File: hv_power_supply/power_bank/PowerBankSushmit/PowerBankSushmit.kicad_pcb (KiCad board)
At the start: 2 copper layers, 43 parts, among them J1 NanoFit_RA_TH_02, J2 NanoFit_RA_TH_02, J3 USB-A-S-X-X-SM2, Q1 SSM3K333R, U1 USB_MicroB, U2 MCP73871T-2CCI_ML, U3 - Boost Converter TPS61090RSAR

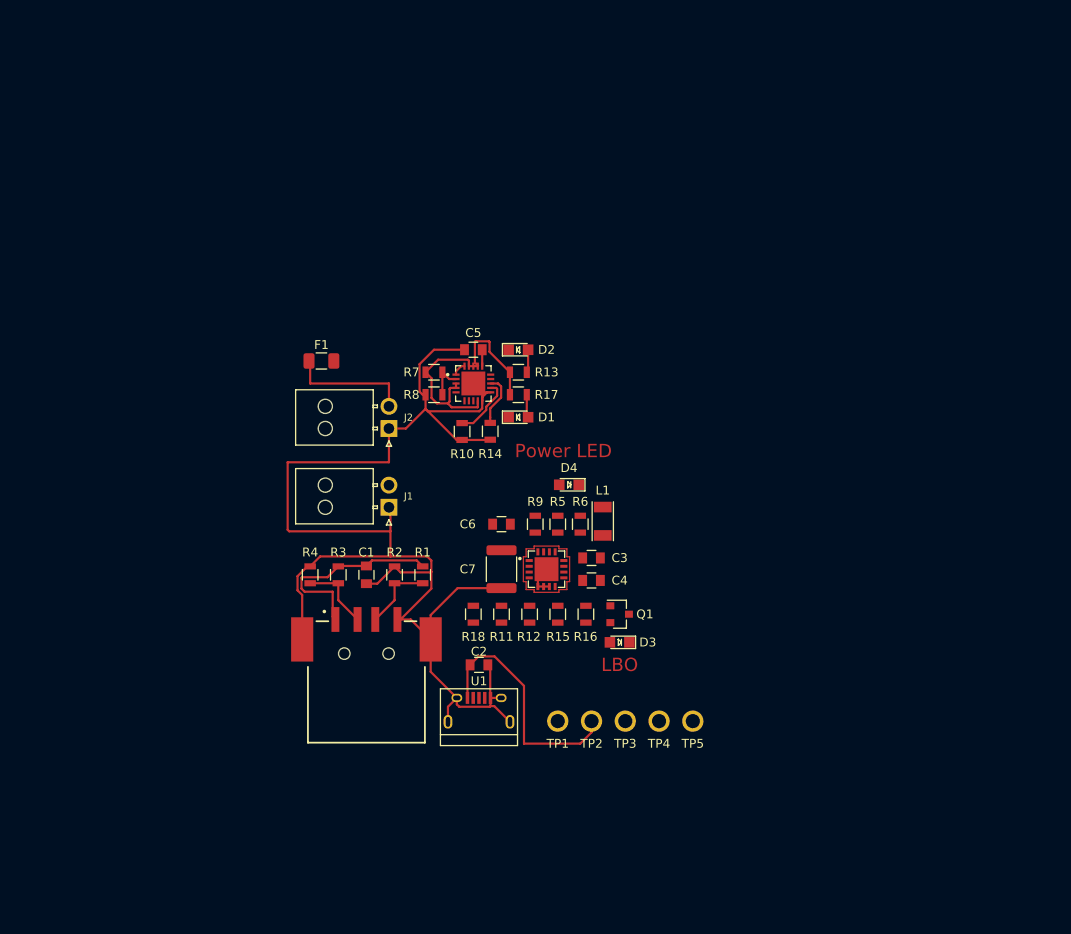
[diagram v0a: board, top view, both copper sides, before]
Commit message: Tried working on the main charging path
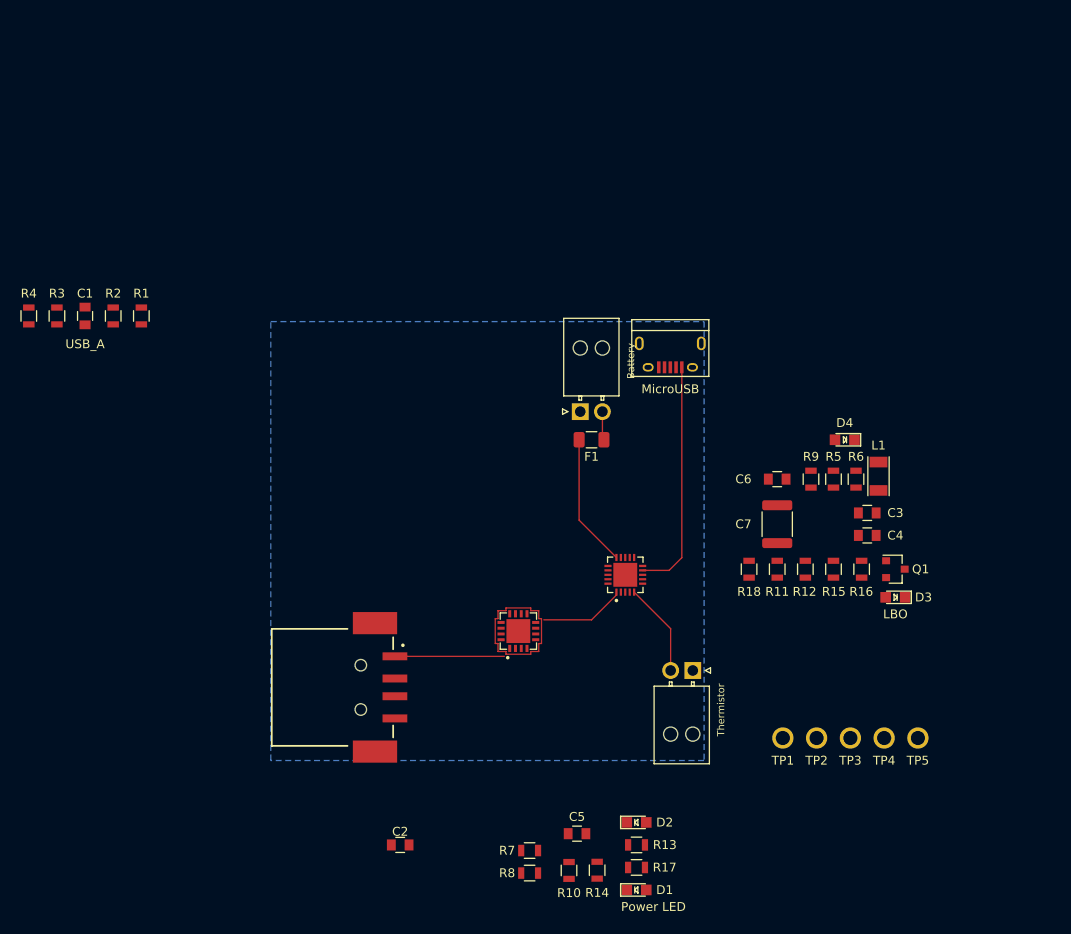
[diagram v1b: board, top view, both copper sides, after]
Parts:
- moved C5 55.8 mm to (207.9, 132.1)
- moved R7 55.0 mm to (202.6, 134.0)
- moved R8 55.0 mm to (202.6, 136.5)
- moved D1 55.0 mm to (214.6, 138.4)
- moved D2 55.0 mm to (214.6, 130.8)
- moved R13 55.0 mm to (214.6, 133.3)
- moved R17 55.0 mm to (214.6, 135.9)
- moved R14 51.0 mm to (210.2, 136.2)
- moved R10 51.0 mm to (207.0, 136.2)
- moved U1 45.5 mm to (218.4, 78.1), turned to 180 degrees
- moved C1 43.1 mm to (152.4, 73.7)
- moved R1 43.1 mm to (158.8, 73.7)
- moved R2 43.1 mm to (155.6, 73.7)
- moved R3 43.1 mm to (149.2, 73.7)
- moved R4 43.1 mm to (146.1, 73.7)
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- renumbered J2 to Battery, J1 to Thermistor
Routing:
- net GND: track 163.3 -> 0.00 mm
- net VBUS: track 58.8 -> 26.5 mm
- net /Battery+: track 0.00 -> 15.0 mm
- net Net-(F1-Pad1): track 14.1 -> 3.25 mm
- net +5V: track 23.0 -> 12.3 mm
- net /16K_Thermistor: track 0.00 -> 10.5 mm
- net Net-(J3-Pad03): track 8.17 -> 0.00 mm
- net Net-(J3-Pad02): track 8.17 -> 0.00 mm
- net +BATT: track 1.57 -> 9.68 mm
- net Net-(R10-Pad1): track 7.00 -> 0.00 mm
- net Net-(R14-Pad1): track 5.94 -> 0.00 mm
- net Net-(R7-Pad2): track 4.40 -> 0.00 mm
- net Net-(D2-Pad2): track 2.60 -> 0.00 mm
- net Net-(D1-Pad2): track 2.60 -> 0.00 mm
- net Net-(C5-Pad1): track 1.86 -> 0.00 mm
- added copper zone on B.Cu, net GND
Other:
- net class Default: clearance 0.2 -> 0.1524; trace_width 0.25 -> 0.1524; via_dia 0.8 -> 0.6096; via_drill 0.4 -> 0.3048
- rule trace_clearance: 0.2 -> 0.1524
- rule trace_min: 0.2 -> 0.1524
- rule via_min_drill: 0.3 -> 0.3048
- rule via_min_size: 0.4 -> 0.1524
- board text added: "MicroUSB"
- board text added: "USB_A"

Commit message: Updated PCB Layout
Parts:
- removed U3 - Boost Converter: TPS61090RSAR, formula:TPS61090RSAR
- added U3: TPS61090RSAR, formula:TPS61090RSAR, F.Cu at (203.2, 116.8)
- moved R3 60.8 mm to (194.9, 113.7), turned to 180 degrees
- moved R4 60.3 mm to (191.1, 113.7), turned to 0 degrees
- moved R1 56.8 mm to (194.9, 117.5), turned to 180 degrees
- moved R2 56.4 mm to (191.1, 117.5), turned to 0 degrees
- moved C1 53.4 mm to (191.1, 110.5), turned to 180 degrees
- moved TP5 50.0 mm to (201.3, 99.7)
- moved D4 45.4 mm to (207.0, 120.7)
- moved D3 43.8 mm to (200.0, 104.8), turned to 90 degrees
- moved TP4 42.8 mm to (202.6, 106.2)
- moved L1 42.8 mm to (208.3, 118.1), turned to 180 degrees
- moved Q1 42.1 mm to (202.6, 110.5), turned to 90 degrees
- moved C6 41.5 mm to (198.8, 118.7), turned to 0 degrees
- moved R6 39.5 mm to (206.4, 113.7), turned to 0 degrees
- moved TP1 38.4 mm to (194.9, 108.6)
- moved R12 37.0 mm to (198.8, 114.3), turned to 180 degrees
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- renumbered Thermistor to J1, Battery to J2
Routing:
- net +5V: track 12.3 -> 34.4 mm
- net +BATT: track 9.68 -> 28.8 mm
- net Net-(Q1-Pad1): track 0.00 -> 15.6 mm
- net /Battery+: track 15.0 -> 27.7 mm
- net Net-(R9-Pad1): track 0.00 -> 11.6 mm
- net VBUS: track 26.5 -> 17.4 mm
- net Net-(D3-Pad2): track 0.00 -> 7.78 mm
- net Net-(J3-Pad03): track 0.00 -> 7.73 mm
- net Net-(J3-Pad02): track 0.00 -> 7.73 mm
- net Net-(D3-Pad1): track 0.00 -> 4.62 mm
- net Net-(D1-Pad1): track 0.00 -> 3.84 mm
- net Net-(R5-Pad2): track 0.00 -> 3.66 mm
- net Net-(R11-Pad2): track 0.00 -> 3.57 mm
- net Net-(R7-Pad2): track 0.00 -> 3.50 mm
- net Net-(L1-Pad2): track 0.00 -> 3.44 mm
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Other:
- board text added: "->"
- board text removed: "MicroUSB"

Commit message: Updated PCB Layout
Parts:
- removed D4: LED_0805, formula:LED_0805_OEM
- removed J1, J2: NanoFit_RA_TH_02, formula:NanoFit_Molex_1x02x2.50mm_Angled_OEM
- removed TP1, TP2, TP3, TP4, TP5: TP, formula:tp_1.6mm
- added +BATT: TP, formula:tp_1.6mm, F.Cu at (236.9, 69.8)
- added +Batt: TP, formula:tp_1.6mm, F.Cu at (217.2, 50.2)
- added Battery: NanoFit_RA_TH_02, formula:NanoFit_Molex_1x02x2.50mm_Angled_OEM, F.Cu at (249.6, 50.8)
- added Battery+: TP, formula:tp_1.6mm, F.Cu at (243.2, 48.3)
- added LBO: TP, formula:tp_1.6mm, F.Cu at (213.1, 57.1)
- added Power : LED_0805, formula:LED_0805_OEM, F.Cu at (226.7, 57.8)
- added Thermistor: NanoFit_RA_TH_02, formula:NanoFit_Molex_1x02x2.50mm_Angled_OEM, F.Cu at (249.6, 58.4)
- added VBUS: TP, formula:tp_1.6mm, F.Cu at (240.7, 69.8)
- U1: value USB_MicroB -> USB-Micro-1981568-1; footprint formula:USB_Micro-B -> formula:TE_1981568-1
- moved F1 78.7 mm to (246.4, 51.6), turned to 90 degrees
- moved R6 67.8 mm to (218.4, 47.0), turned to 270 degrees
- moved R5 66.3 mm to (220.3, 47.0), turned to 270 degrees
- moved L1 65.7 mm to (227.3, 55.2)
- moved R2 64.5 mm to (229.2, 65.4)
- moved R1 64.5 mm to (229.2, 62.9), turned to 0 degrees
- moved R18 64.3 mm to (225.4, 60.3)
- moved C3 63.7 mm to (221.6, 52.1), turned to 180 degrees
- moved C4 63.7 mm to (221.6, 50.2), turned to 180 degrees
- moved U3 63.1 mm to (221.6, 56.5), turned to 180 degrees
- moved D1 61.1 mm to (245.7, 55.2), turned to 180 degrees
- moved J3 60.6 mm to (226.1, 72.4), turned to 0 degrees
- moved R16 59.5 mm to (214.0, 48.9)
- moved R3 59.2 mm to (225.4, 62.9), turned to 0 degrees
- moved R4 59.2 mm to (225.4, 65.4), turned to 180 degrees
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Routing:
- net GND: track 0.17 -> 148.0 mm, vias 0 -> 6
- net /Battery+: track 27.7 -> 13.8 mm
- net +BATT: track 28.8 -> 41.9 mm
- net Net-(R5-Pad2): track 3.66 -> 14.2 mm
- net VBUS: track 17.4 -> 27.6 mm, vias 0 -> 3
- net Net-(R11-Pad2): track 3.57 -> 11.3 mm
- net Net-(D1-Pad1): track 3.84 -> 11.2 mm
- net Net-(Q1-Pad1): track 15.6 -> 8.92 mm
- net Net-(D2-Pad1): track 2.55 -> 8.79 mm
- net Net-(R14-Pad1): track 1.80 -> 7.49 mm
- net Net-(D3-Pad2): track 7.78 -> 3.48 mm
- net Net-(R9-Pad1): track 11.6 -> 8.23 mm
- net Net-(R10-Pad1): track 1.86 -> 4.64 mm
- net Net-(C5-Pad1): track 0.00 -> 2.69 mm
- net Net-(R7-Pad2): track 3.50 -> 6.07 mm
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- added copper zone on F.Cu, net +5V
- added copper zone on F.Cu, net +BATT
- added copper zone on F.Cu, net /Battery+
- added copper zone on B.Cu, net VBUS
- added copper zone on F.Cu, net VBUS
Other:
- board outline added: 48.3 x 30.5 mm
- board text added: "DIY Power Bank Olin Electric Motorsports 12/20 Sushmit Dutta"
- board text removed: "->"
- board text removed: "LBO"
- board text removed: "Power LED"
- board text removed: "USB_A"

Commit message: Phase 3.0 (New Copper Planes)
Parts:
- moved C6 9.53 mm to (226.1, 57.8), turned to 0 degrees
- moved R18 4.84 mm to (229.9, 58.4), turned to 90 degrees
- moved Power  4.49 mm to (229.9, 54.6), turned to 270 degrees
- moved C5 2.62 mm to (238.1, 64.8)
- moved J3 2.01 mm to (225.4, 70.5)
- moved R2 1.91 mm to (229.2, 63.5)
- moved R4 1.91 mm to (225.4, 63.5), turned to 0 degrees
- moved R1 1.27 mm to (229.2, 61.6)
- moved R3 1.27 mm to (225.4, 61.6)
- moved L1 1.27 mm to (227.3, 54.0), turned to 270 degrees
- moved C1 0.64 mm to (215.3, 67.3)
- moved C3 0.63 mm to (221.6, 52.7), turned to 0 degrees
- moved C4 0.63 mm to (221.6, 50.8), turned to 0 degrees
- moved C7 0.63 mm to (219.1, 61.6)
- moved U2 0.63 mm to (240.0, 61.0)
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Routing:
- net +BATT: track 41.9 -> 25.3 mm
- net +5V: track 32.2 -> 18.5 mm
- net GND: track 148.0 -> 140.3 mm, vias 6 -> 8
- net Net-(R5-Pad2): track 14.2 -> 11.3 mm
- net /16K_Thermistor: track 7.70 -> 10.2 mm
- net VBUS: track 27.6 -> 26.0 mm, vias 3 -> 11
- net Net-(D4-Pad2): track 3.13 -> 1.76 mm
- net Net-(L1-Pad2): track 2.93 -> 2.11 mm
- net Net-(J3-Pad02): track 6.22 -> 7.03 mm
- net Net-(C5-Pad1): track 2.69 -> 1.89 mm
- net Net-(R7-Pad2): track 6.07 -> 6.70 mm
- net Net-(R10-Pad1): track 4.64 -> 4.01 mm
- net Net-(R14-Pad1): track 7.49 -> 6.89 mm
- net /Battery+: track 13.8 -> 13.2 mm
- added copper zone on F.Cu, net Net-(L1-Pad2)

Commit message: Changes based on last comments
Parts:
- Boost Converter: renamed from U3
- Load Manager: renamed from U2
- moved L1 1.27 mm to (226.1, 54.0)
- moved R10 0.13 mm to (238.1, 57.0)
- moved R14 0.13 mm to (238.1, 55.1)
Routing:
- net GND: track 140.3 -> 143.6 mm, vias 8 -> 10
- net Net-(L1-Pad2): track 2.11 -> 4.47 mm
- net +5V: track 18.5 -> 20.1 mm
- added copper zone on F.Cu, net (none)
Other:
- board text added: "DIY Power Bank Olin Electric Motorsports 01/21 Sushmit Dutta"
- board text removed: "DIY Power Bank Olin Electric Motorsports 12/20 Sushmit Dutta"
